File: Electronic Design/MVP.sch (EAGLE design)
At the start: 31 parts, among them IC1 ACS711KLCTR-12AB-T, IC3 ATMEGA328-PU, Q2 16MHz, Q3 IRF9540, Q4 IRF9540

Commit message: All components routed sucessfully
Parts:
- R14: device resistor:R-EU_R1210 -> resistor:R-EU_VTA52
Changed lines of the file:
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@@
 <setting verticaltext="up"/>
 </settings>
-<grid distance="0.05" unitdist="inch" unit="inch" style="lines" multiple="1" display="no" altdistance="0.01" altunitdist="inch" altunit="inch"/>
+<grid distance="0.1" unitdist="inch" unit="inch" style="lines" multiple="1" display="no" altdistance="0.01" altunitdist="inch" altunit="inch"/>
 <layers>
-<layer number="1" name="Top" color="4" fill="1" visible="yes" active="no"/>
-<layer number="16" name="Bottom" color="1" fill="1" visible="yes" active="no"/>
-<layer number="17" name="Pads" color="2" fill="1" visible="yes" active="no"/>
-<layer number="18" name="Vias" color="2" fill="1" visible="yes" active="no"/>
-<layer number="19" name="Unrouted" color="6" fill="1" visible="yes" active="no"/>
-<layer number="20" name="Dimension" color="15" fill="1" visible="yes" active="no"/>
-<layer number="21" name="tPlace" color="7" fill="1" visible="yes" active="no"/>
-<layer number="22" name="bPlace" color="7" fill="1" visible="yes" active="no"/>
-<layer number="23" name="tOrigins" color="15" fill="1" visible="yes" active="no"/>
-<layer number="24" name="bOrigins" color="15" fill="1" visible="yes" active="no"/>
-<layer number="25" name="tNames" color="7" fill="1" visible="yes" active="no"/>
-<layer number="26" name="bNames" color="7" fill="1" visible="yes" active="no"/>
-<layer number="27" name="tValues" color="7" fill="1" visible="yes" active="no"/>
-<layer number="28" name="bValues" color="7" fill="1" visible="yes" active="no"/>
+<layer number="1" name="Top" color="4" fill="1" visible="no" active="no"/>
+<layer number="16" name="Bottom" color="1" fill="1" visible="no" active="no"/>
+<layer number="17" name="Pads" color="2" fill="1" visible="no" active="no"/>
+<layer number="18" name="Vias" color="2" fill="1" visible="no" active="no"/>
+<layer number="19" name="Unrouted" color="6" fill="1" visible="no" active="no"/>
+<layer number="20" name="Dimension" color="15" fill="1" visible="no" active="no"/>
+<layer number="21" name="tPlace" color="7" fill="1" visible="no" active="no"/>
+<layer number="22" name="bPlace" color="7" fill="1" visible="no" active="no"/>
+<layer number="23" name="tOrigins" color="15" fill="1" visible="no" active="no"/>
+<layer number="24" name="bOrigins" color="15" fill="1" visible="no" active="no"/>
+<layer number="25" name="tNames" color="7" fill="1" visible="no" active="no"/>
+<layer number="26" name="bNames" color="7" fill="1" visible="no" active="no"/>
+<layer number="27" name="tValues" color="7" fill="1" visible="no" active="no"/>
+<layer number="28" name="bValues" color="7" fill="1" visible="no" active="no"/>
 <layer number="29" name="tStop" color="7" fill="3" visible="no" active="no"/>
 <layer number="30" name="bStop" color="7" fill="6" visible="no" active="no"/>
@@
 <layer number="35" name="tGlue" color="7" fill="4" visible="no" active="no"/>
 <layer number="36" name="bGlue" color="7" fill="5" visible="no" active="no"/>
-<layer number="37" name="tTest" color="7" fill="1" visible="yes" active="no"/>
-<layer number="38" name="bTest" color="7" fill="1" visible="yes" active="no"/>
+<layer number="37" name="tTest" color="7" fill="1" visible="no" active="no"/>
+<layer number="38" name="bTest" color="7" fill="1" visible="no" active="no"/>
 <layer number="39" name="tKeepout" color="4" fill="11" visible="no" active="no"/>
 <layer number="40" name="bKeepout" color="1" fill="11" visible="no" active="no"/>
@@
 <layer number="44" name="Drills" color="7" fill="1" visible="no" active="no"/>
 <layer number="45" name="Holes" color="7" fill="1" visible="no" active="no"/>
-<layer number="46" name="Milling" color="3" fill="1" visible="yes" active="no"/>
-<layer number="47" name="Measures" color="7" fill="1" visible="yes" active="no"/>
-<layer number="48" name="Document" color="7" fill="1" visible="yes" active="no"/>
-<layer number="49" name="Reference" color="7" fill="1" visible="yes" active="no"/>
-<layer number="50" name="dxf" color="7" fill="1" visible="yes" active="no"/>
-<layer number="51" name="tDocu" color="7" fill="1" visible="yes" active="no"/>
-<layer number="52" name="bDocu" color="7" fill="1" visible="yes" active="no"/>
-<layer number="53" name="tGND_GNDA" color="7" fill="9" visible="yes" active="no"/>
-<layer number="54" name="bGND_GNDA" color="1" fill="9" visible="yes" active="no"/>
-<layer number="56" name="wert" color="7" fill="1" visible="yes" active="no"/>
+<layer number="46" name="Milling" color="3" fill="1" visible="no" active="no"/>
+<layer number="47" name="Measures" color="7" fill="1" visible="no" active="no"/>
+<layer number="48" name="Document" color="7" fill="1" visible="no" active="no"/>
+<layer number="49" name="Reference" color="7" fill="1" visible="no" active="no"/>
+<layer number="50" name="dxf" color="7" fill="1" visible="no" active="no"/>
+<layer number="51" name="tDocu" color="7" fill="1" visible="no" active="no"/>
+<layer number="52" name="bDocu" color="7" fill="1" visible="no" active="no"/>
+<layer number="53" name="tGND_GNDA" color="7" fill="9" visible="no" active="no"/>
+<layer number="54" name="bGND_GNDA" color="1" fill="9" visible="no" active="no"/>
+<layer number="56" name="wert" color="7" fill="1" visible="no" active="no"/>
 <layer number="90" name="Modules" color="5" fill="1" visible="yes" active="yes"/>
 <layer number="91" name="Nets" color="2" fill="1" visible="yes" active="yes"/>
@@
 <part name="Q4" library="transistor-power" deviceset="PMOSFET_P" device="TO220BV" value="IRF9540"/>
 <part name="R12" library="resistor" deviceset="R-TRIMM" device="4G/J" value="4.7k"/>
-<part name="R14" library="resistor" deviceset="R-EU_" device="R1210" value="1k"/>
+<part name="R14" library="resistor" deviceset="R-EU_" device="VTA52" value="1k"/>
 <part name="SUPPLY22" library="supply2" deviceset="GND" device=""/>
 <part name="SUPPLY23" library="supply2" deviceset="GND" device=""/>

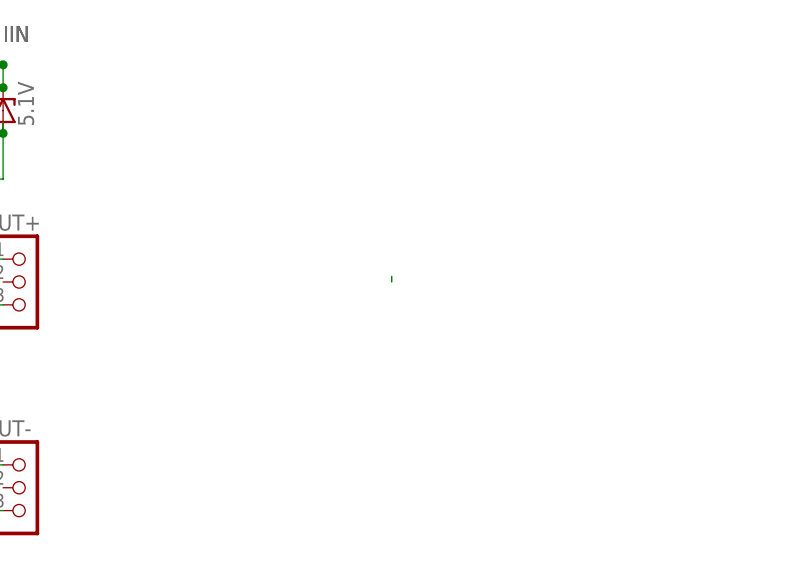
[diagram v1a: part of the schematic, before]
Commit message: Adding switch and resistors for power measurement mode
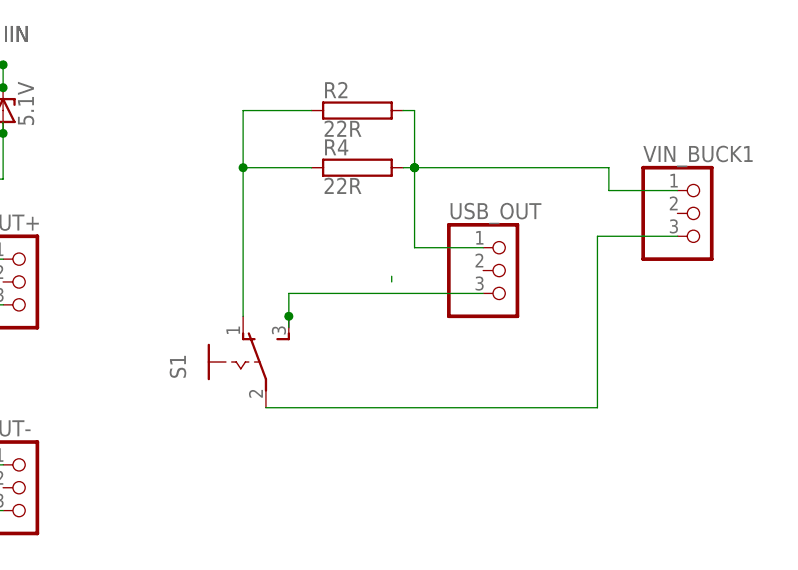
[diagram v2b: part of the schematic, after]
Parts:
- added R2, R4: 22R, resistor-power:RRWM8X45
- added S1: (no value), switch:255SB
- added USB_OUT, VIN_BUCK1: (no value), pinhead:PINHD-1X3
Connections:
- new net N$22: S1.P, VIN_BUCK1.3
- new net N$23: R2.2, R4.2, USB_OUT.1, VIN_BUCK1.1
- new net N$24: R2.1, R4.1, S1.O
- new net N$25: S1.S, USB_OUT.3
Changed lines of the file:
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@@
 <setting verticaltext="up"/>
 </settings>
-<grid distance="0.1" unitdist="inch" unit="inch" style="lines" multiple="1" display="no" altdistance="0.01" altunitdist="inch" altunit="inch"/>
+<grid distance="0.05" unitdist="inch" unit="inch" style="lines" multiple="1" display="no" altdistance="0.01" altunitdist="inch" altunit="inch"/>
 <layers>
 <layer number="1" name="Top" color="4" fill="1" visible="no" active="no"/>
@@
 <part name="SUPPLY6" library="supply2" deviceset="GND" device=""/>
 <part name="C3" library="resistor" deviceset="C-EU" device="C1210" value="10u"/>
+<part name="VIN_BUCK1" library="pinhead" deviceset="PINHD-1X3" device=""/>
+<part name="R2" library="resistor-power" deviceset="R" device="RWM8X45" value="22R"/>
+<part name="R4" library="resistor-power" deviceset="R" device="RWM8X45" value="22R"/>
+<part name="S1" library="switch" deviceset="255SB" device=""/>
+<part name="USB_OUT" library="pinhead" deviceset="PINHD-1X3" device=""/>
 </parts>
 <sheets>
@@
 <instance part="SUPPLY6" gate="GND" x="5.08" y="13.97"/>
 <instance part="C3" gate="G$1" x="31.75" y="35.56"/>
+<instance part="VIN_BUCK1" gate="A" x="115.57" y="93.98"/>
+<instance part="R2" gate="G$1" x="77.47" y="105.41"/>
+<instance part="R4" gate="G$1" x="77.47" y="99.06"/>
+<instance part="S1" gate="1" x="64.77" y="77.47"/>
+<instance part="USB_OUT" gate="A" x="93.98" y="87.63"/>
 </instances>
 <busses>
@@
 </segment>
 </net>
+<net name="N$22" class="0">
+<segment>
+<pinref part="S1" gate="1" pin="P"/>
+<wire x1="67.31" y1="72.39" x2="104.14" y2="72.39" width="0.1524" layer="91"/>
+<wire x1="104.14" y1="72.39" x2="104.14" y2="91.44" width="0.1524" layer="91"/>
+<pinref part="VIN_BUCK1" gate="A" pin="3"/>
+<wire x1="113.03" y1="91.44" x2="104.14" y2="91.44" width="0.1524" layer="91"/>
+</segment>
+</net>
+<net name="N$23" class="0">
+<segment>
+<pinref part="R2" gate="G$1" pin="2"/>
+<wire x1="82.55" y1="105.41" x2="83.82" y2="105.41" width="0.1524" layer="91"/>
+<wire x1="83.82" y1="105.41" x2="83.82" y2="99.06" width="0.1524" layer="91"/>
+<wire x1="83.82" y1="99.06" x2="105.41" y2="99.06" width="0.1524" layer="91"/>
+<pinref part="R4" gate="G$1" pin="2"/>
+<wire x1="82.55" y1="99.06" x2="83.82" y2="99.06" width="0.1524" layer="91"/>
+<wire x1="83.82" y1="99.06" x2="83.82" y2="90.17" width="0.1524" layer="91"/>
+<pinref part="USB_OUT" gate="A" pin="1"/>
+<wire x1="83.82" y1="90.17" x2="91.44" y2="90.17" width="0.1524" layer="91"/>
+<junction x="83.82" y="99.06"/>
+<junction x="83.82" y="99.06"/>
+<pinref part="VIN_BUCK1" gate="A" pin="1"/>
+<wire x1="113.03" y1="96.52" x2="105.41" y2="96.52" width="0.1524" layer="91"/>
+<wire x1="105.41" y1="96.52" x2="105.41" y2="99.06" width="0.1524" layer="91"/>
+</segment>
+</net>
+<net name="N$24" class="0">
+<segment>
+<pinref part="R2" gate="G$1" pin="1"/>
+<wire x1="72.39" y1="105.41" x2="64.77" y2="105.41" width="0.1524" layer="91"/>
+<wire x1="64.77" y1="105.41" x2="64.77" y2="99.06" width="0.1524" layer="91"/>
+<pinref part="R4" gate="G$1" pin="1"/>
+<wire x1="64.77" y1="99.06" x2="72.39" y2="99.06" width="0.1524" layer="91"/>
+<pinref part="S1" gate="1" pin="O"/>
+<wire x1="64.77" y1="99.06" x2="64.77" y2="82.55" width="0.1524" layer="91"/>
+<junction x="64.77" y="99.06"/>
+</segment>
+</net>
+<net name="N$25" class="0">
+<segment>
+<pinref part="USB_OUT" gate="A" pin="3"/>
+<wire x1="91.44" y1="85.09" x2="69.85" y2="85.09" width="0.1524" layer="91"/>
+<wire x1="69.85" y1="85.09" x2="69.85" y2="82.55" width="0.1524" layer="91"/>
+<pinref part="S1" gate="1" pin="S"/>
+<wire x1="69.85" y1="82.55" x2="69.85" y2="81.28" width="0.1524" layer="91"/>
+<junction x="69.85" y="82.55"/>
+</segment>
+</net>
